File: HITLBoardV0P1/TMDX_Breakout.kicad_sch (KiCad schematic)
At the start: 1 part, among them U1 TMDX570LC43HDK_Connectors

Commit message: UPDATE -- IN PROGRESS
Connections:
- net +12V: now reaches U1.P10-1 (EXP_12V)
- net +12V: now also U1.P10-65 (EXP_12V), U1.P11-1 (EXP_12V), U1.P11-3 (EXP_12V), U1.P9-1 (EXP_12V), U1.P9-3 (EXP_12V), U1.P9-65 (EXP_12V)
- net GND: now reaches U1.P10-2 (GND)
- net GND: now also U1.P10-29 (GND), U1.P10-30 (GND), U1.P10-39 (GND), U1.P10-40 (GND), U1.P10-57 (GND), U1.P10-58 (GND), U1.P10-66 (GND), U1.P9-13 (GND), U1.P9-14 (GND), U1.P9-2 (GND), U1.P9-29 (GND), U1.P9-30 (GND), U1.P9-39 (GND), U1.P9-4 (GND), U1.P9-40 (GND), U1.P9-49 (GND), U1.P9-50 (GND), U1.P9-59 (GND), U1.P9-66 (GND)
- net GIOA_1: now reaches U1.P11-19 (GIOA_1)
- net GIOA_3: now reaches U1.P11-21 (GIOA_3)
- net GIOA_5: now reaches U1.P11-23 (GIOA_5)
- net GIOA_7: now reaches U1.P11-25 (GIOA_7)
- net GIOB_1: now reaches U1.P11-27 (GIOB_1)
- net GIOB_3: now reaches U1.P11-29 (GIOB_3)
- net GIOB_5: now reaches U1.P11-31 (GIOB_5)
- net SPI1_SIMO: now reaches U1.P9-11 (SPI1_SIMO)
- net SPI1_SOMI: now reaches U1.P9-12 (SPI1_SOMI)
- net SPI1_CLK: now reaches U1.P9-6 (SPI1_CLK)
- net SPI1_CS1: now reaches U1.P9-7 (SPI1_CS1_NHET117)
- net SPI1_CS0_N: now reaches U1.P9-8 (SPI1_CS0_N)
- net SCI4_TX renamed SCI4_TXX

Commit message: update to board with spi buses assigned
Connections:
- net SPI5_SCLK: now reaches U1.P9-16 (SPI5_CLK)
- net SPI5_CS1_NR: now reaches U1.P9-17 (SPI5_CS1_N)
- net SPI5_CS0_N: now reaches U1.P9-18 (SPI5_CS0_N)
- net SPI5_SIMO_0: now reaches U1.P9-21 (SPI5_SIMO_0)
- net SPI5_SOMI_0: now reaches U1.P9-22 (SPI5_SOMI_0)
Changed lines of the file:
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@@
+		)
+	)
+	(wire
+		(pts
+			(xy 105.41 46.99) (xy 119.38 46.99)
+		)
+		(stroke
+			(width 0)
+			(type default)
 		)
 	)
@@
 		)
 	)
+	(hierarchical_label "SPI5_SOMI_0"
+		(shape input)
+		(at 119.38 54.61 0)
+		(effects
+			(font
+				(size 1.27 1.27)
+			)
+			(justify left)
+		)
+	)
+	(hierarchical_label "SPI5_SIMO_0"
+		(shape input)
+		(at 35.56 54.61 180)
+		(effects
+			(font
+				(size 1.27 1.27)
+			)
+			(justify right)
+		)
+	)
+	(hierarchical_label "SPI5_CS1_NR"
+		(shape input)
+		(at 35.56 49.53 180)
+		(effects
+			(font
+				(size 1.27 1.27)
+			)
+			(justify right)
+		)
+	)
 	(hierarchical_label "GIOA_7"
 		(shape input)
@@
 		)
 	)
+	(hierarchical_label "SPI5_CS0_N"
+		(shape input)
+		(at 119.38 49.53 0)
+		(effects
+			(font
+				(size 1.27 1.27)
+			)
+			(justify left)
+		)
+	)
 	(hierarchical_label "GIOA_1"
 		(shape input)
@@
 		)
 	)
+	(hierarchical_label "SPI5_SCLK"
+		(shape input)
+		(at 119.38 46.99 0)
+		(effects
+			(font
+				(size 1.27 1.27)
+			)
+			(justify left)
+		)
+	)

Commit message: add debug LEDs and reset_n button for system reset
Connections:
- net GIOB_7: now reaches U1.P11-33 (GIOB_7)
- net POR_RESET_N: now reaches U1.P9-60 (POR_RST_N)
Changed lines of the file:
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@@
+	(wire
+		(pts
+			(xy 105.41 102.87) (xy 121.92 102.87)
+		)
+		(stroke
+			(width 0)
+			(type default)
+		)
+	)
+	(wire
+		(pts
+			(xy 154.94 182.88) (xy 173.99 182.88)
+		)
+		(stroke
+			(width 0)
+			(type default)
+		)
+	)
 	(wire
 		(pts
@@
 		)
 	)
+	(hierarchical_label "GIOB_7"
+		(shape input)
+		(at 154.94 182.88 180)
+		(effects
+			(font
+				(size 1.27 1.27)
+			)
+			(justify right)
+		)
+	)
 	(hierarchical_label "SCI4_RX"
 		(shape input)
@@
 		(effects
 			(font
+				(size 1.27 1.27)
+			)
+			(justify left)
+		)
+	)
+	(hierarchical_label "POR_RESET_N"
+		(shape input)
+		(at 121.92 102.87 0)
+		(effects
+			(font

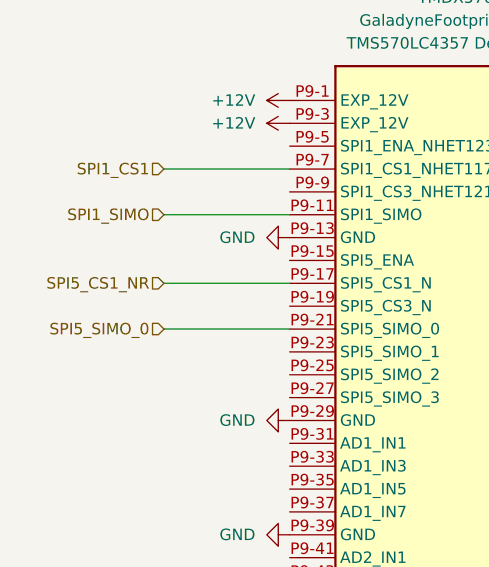
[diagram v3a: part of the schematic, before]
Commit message: MINOR UPDATES -- SWTICH ONE LAN TO SPI 5 INSTEAD OF SPI1 ON THE TMDX, SET UP LAN8650S for actual differential pair routing by changing suffix to "_DN" and "_DP" instead of "_N" or "_P" or just "N", "P"
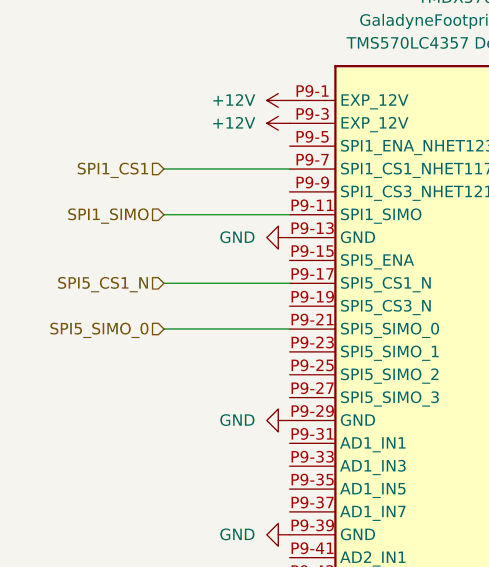
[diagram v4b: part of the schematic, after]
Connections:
- net SPI5_CS1_NR renamed SPI5_CS1_N
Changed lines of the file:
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@@
 		)
 	)
-	(hierarchical_label "SPI5_CS1_NR"
+	(hierarchical_label "SPI5_CS1_N"
 		(shape input)
 		(at 35.56 49.53 180)

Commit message: FIX spi 3 on tmdx for current loop ADC, add gpio pin for data ready
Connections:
- net SPI3_SIMO: now reaches U1.P11-73 (SPI3_SIMO)
- net SPI3_SOMI: now reaches U1.P11-74 (SPI3_SOMI)
- net SPI3_CS1_N: now reaches U1.P11-75 (SPI3_CS1_NHET125)
- net SPI3_SCLK: now reaches U1.P11-78 (SPI3_CLK)
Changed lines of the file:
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@@
+	(wire
+		(pts
+			(xy 152.4 236.22) (xy 173.99 236.22)
+		)
+		(stroke
+			(width 0)
+			(type default)
+		)
+	)
+	(wire
+		(pts
+			(xy 152.4 233.68) (xy 173.99 233.68)
+		)
+		(stroke
+			(width 0)
+			(type default)
+		)
+	)
+	(wire
+		(pts
+			(xy 243.84 233.68) (xy 264.16 233.68)
+		)
+		(stroke
+			(width 0)
+			(type default)
+		)
+	)
 	(wire
 		(pts
@@
 		(pts
 			(xy 154.94 177.8) (xy 173.99 177.8)
+		)
+		(stroke
+			(width 0)
+			(type default)
+		)
+	)
+	(wire
+		(pts
+			(xy 243.84 238.76) (xy 264.16 238.76)
 		)
 		(stroke
@@
 		)
 	)
+	(label "SPI3_SIMO"
+		(at 154.94 233.68 0)
+		(effects
+			(font
+				(size 1.27 1.27)
+			)
+			(justify left bottom)
+		)
+	)
 	(label "SCI4_TX"
 		(at 156.21 210.82 0)
@@
 		)
 	)
+	(label "SPI3_CS1_N"
+		(at 154.94 236.22 0)
+		(effects
+			(font
+				(size 1.27 1.27)
+			)
+			(justify left bottom)
+		)
+	)
 	(label "SCI3_TX"
 		(at 156.21 203.2 0)
@@
 		)
 	)
+	(label "SPI3_SOMI"
+		(at 248.92 233.68 0)
+		(effects
+			(font
+				(size 1.27 1.27)
+			)
+			(justify left bottom)
+		)
+	)
 	(label "SCI3_RX"
 		(at 250.19 195.58 0)
@@
 		)
 	)
+	(label "SPI3_CLK"
+		(at 248.92 238.76 0)
+		(effects
+			(font
+				(size 1.27 1.27)
+			)
+			(justify left bottom)
+		)
+	)
 	(label "SCI1_TX"
 		(at 250.19 147.32 0)
@@
 		)
 	)
+	(hierarchical_label "SPI3_SIMO"
+		(shape input)
+		(at 152.4 233.68 180)
+		(effects
+			(font
+				(size 1.27 1.27)
+			)
+			(justify right)
+		)
+	)
+	(hierarchical_label "SPI3_SCLK"
+		(shape input)
+		(at 264.16 238.76 0)
+		(effects
+			(font
+				(size 1.27 1.27)
+			)
+			(justify left)
+		)
+	)
 	(hierarchical_label "GIOB_7"
 		(shape input)
@@
 		(effects
 			(font
+				(size 1.27 1.27)
+			)
+			(justify left)
+		)
+	)
+	(hierarchical_label "SPI3_CS1_N"
+		(shape input)
+		(at 152.4 236.22 180)
+		(effects
+			(font
+				(size 1.27 1.27)
+			)
+			(justify right)
+		)
+	)
+	(hierarchical_label "SPI3_SOMI"
+		(shape input)
+		(at 264.16 233.68 0)
+		(effects
+			(font
